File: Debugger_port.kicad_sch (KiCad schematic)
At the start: 6 parts, among them J10 Conn_01x06_Female

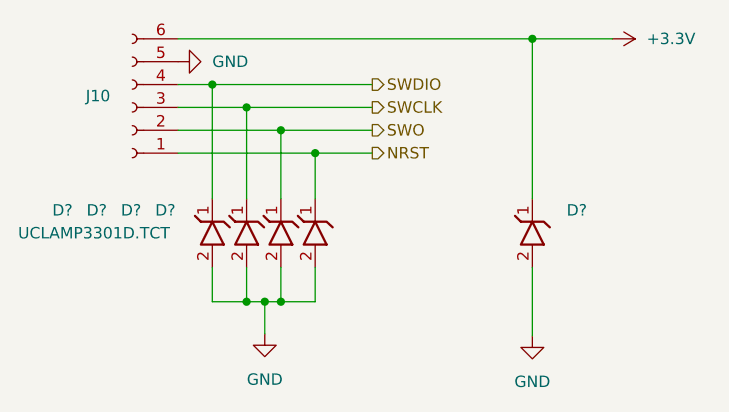
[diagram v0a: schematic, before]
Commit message: updated footprints on board and sgematics
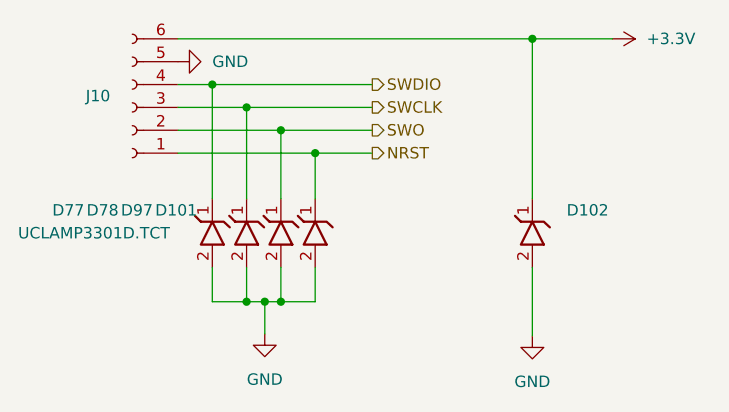
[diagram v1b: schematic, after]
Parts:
- gave numbers to parts that had none: 5
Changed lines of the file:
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@@
   (symbol (lib_id "_Diodes:UCLAMP3301D.TCT") (at 154.94 118.11 0) (unit 1)
     (in_bom yes) (on_board yes)
-    (property "Reference" "D?" (id 0) (at 137.16 107.95 0)
+    (property "Reference" "D97" (id 0) (at 137.16 107.95 0)
       (effects (font (size 1.27 1.27)) (justify left))
     )
@@
   (symbol (lib_id "_Diodes:UCLAMP3301D.TCT") (at 182.88 118.11 0) (unit 1)
     (in_bom yes) (on_board yes)
-    (property "Reference" "D?" (id 0) (at 186.69 107.95 0)
+    (property "Reference" "D102" (id 0) (at 186.69 107.95 0)
       (effects (font (size 1.27 1.27)) (justify left))
     )
@@
   (symbol (lib_id "_Diodes:UCLAMP3301D.TCT") (at 158.75 118.11 0) (unit 1)
     (in_bom yes) (on_board yes)
-    (property "Reference" "D?" (id 0) (at 140.97 107.95 0)
+    (property "Reference" "D101" (id 0) (at 140.97 107.95 0)
       (effects (font (size 1.27 1.27)) (justify left))
     )
@@
   (symbol (lib_id "_Diodes:UCLAMP3301D.TCT") (at 151.13 118.11 0) (unit 1)
     (in_bom yes) (on_board yes)
-    (property "Reference" "D?" (id 0) (at 133.35 107.95 0)
+    (property "Reference" "D78" (id 0) (at 133.35 107.95 0)
       (effects (font (size 1.27 1.27)) (justify left))
     )
@@
   (symbol (lib_id "_Diodes:UCLAMP3301D.TCT") (at 147.32 118.11 0) (unit 1)
     (in_bom yes) (on_board yes)
-    (property "Reference" "D?" (id 0) (at 129.54 107.95 0)
+    (property "Reference" "D77" (id 0) (at 129.54 107.95 0)
       (effects (font (size 1.27 1.27)) (justify left))
     )
